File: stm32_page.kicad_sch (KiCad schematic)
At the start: 46 parts, among them J1 PZ254V-11-03P_C2937625, J2 PZ254V-11-03P_C2937625, J4 FTSH-107-01-L-DV-K-A, J5 PZ254V-11-03P_C2937625, SW2 6.0*6.0*6.0, SW3 6.0*6.0*6.0, U1 STM32L431KBU6_C2826408, U10 MAX3221ECPWR, X1 SC-32S32.768kHz20PPM7pF

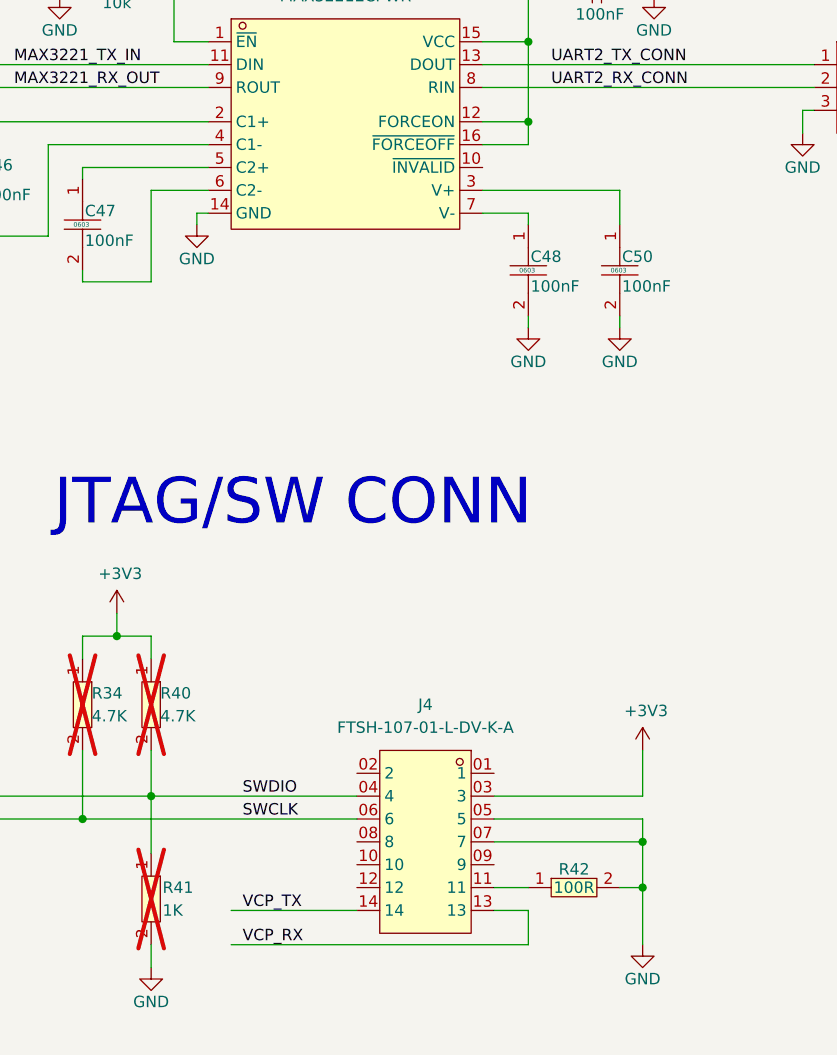
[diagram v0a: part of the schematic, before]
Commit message: replaced part for lower cost
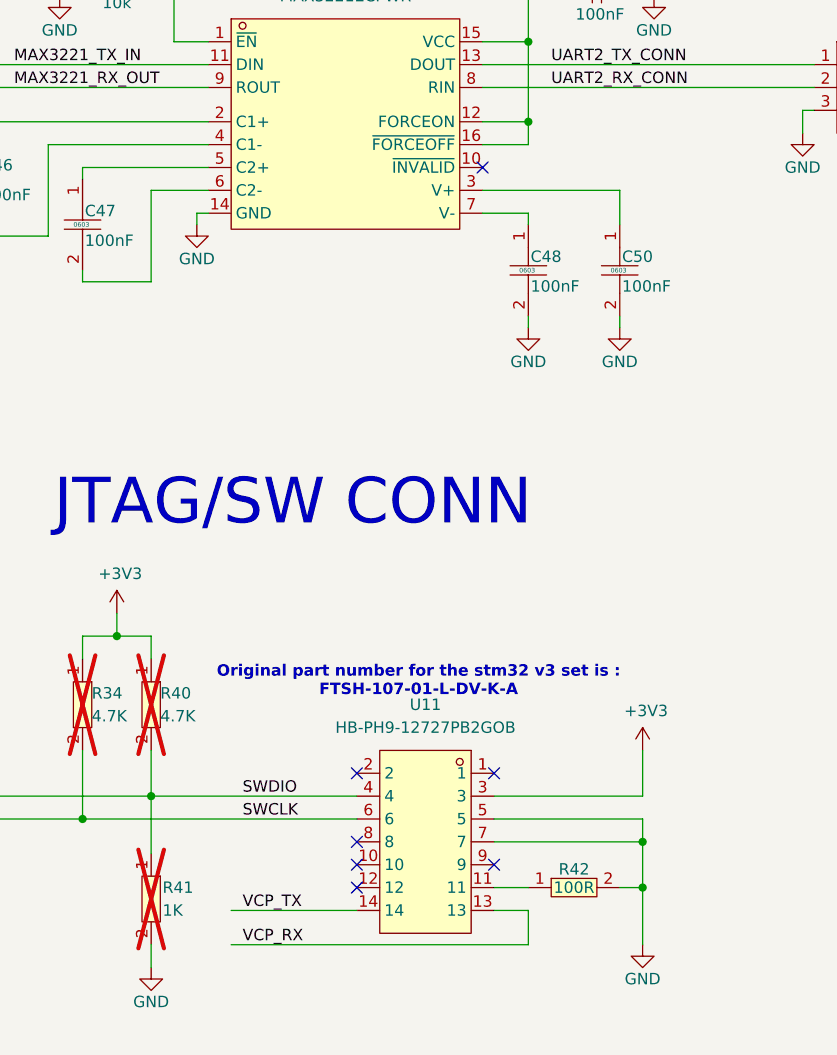
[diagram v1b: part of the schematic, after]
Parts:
- removed J4: FTSH-107-01-L-DV-K-A, easyeda2kicad:HDR-SMD_14P-P1.27_FTSH-107-01-L-DV-K-A, symbol easyeda2kicad:FTSH-107-01-L-DV-K-A
- added U11: HB-PH9-12727PB2GOB, easyeda2kicad:HDR-SMD_14P-P1.27-V-M-R2-C7-LS5.5, symbol easyeda2kicad:HB-PH9-12727PB2GOB
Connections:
- net +3V3: now also U11.3
- net GND: now also U11.5, U11.7
- net SWCLK: now also U11.6
- net SWDIO: now also U11.4
- net VCP_RX: now also U11.13
- net VCP_TX: now also U11.14
- net at R42.1: now also U11.11
- no-connect marks 0 -> 7
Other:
- note added: "Original part number for the stm32 v3 set is : FTSH-107-01-L-DV-K-A"
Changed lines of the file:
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@@
 		)
 	)
+	(text "Original part number for the stm32 v3 set is :\nFTSH-107-01-L-DV-K-A\n"
+		(exclude_from_sim no)
+		(at 338.328 208.28 0)
+		(effects
+			(font
+				(size 1.27 1.27)
+				(thickness 0.254)
+				(bold yes)
+			)
+		)
+	)
 	(text "VBAT"
 		(exclude_from_sim no)
@@
 		(color 0 0 0 0)
 	)
+	(no_connect
+		(at 331.47 228.6)
+	)
+	(no_connect
+		(at 331.47 218.44)
+	)
+	(no_connect
+		(at 346.71 218.44)
+	)
+	(no_connect
+		(at 345.44 151.13)
+	)
+	(no_connect
+		(at 331.47 231.14)
+	)
+	(no_connect
+		(at 331.47 226.06)
+	)
+	(no_connect
+		(at 346.71 228.6)
+	)
 	(wire
 		(pts
@@
 	)
 	(symbol
+		(lib_id "easyeda2kicad:HB-PH9-12727PB2GOB")
+		(at 339.09 226.06 0)
+		(mirror y)
+		(unit 1)
+		(exclude_from_sim no)
+		(in_bom yes)
+		(on_board yes)
+		(dnp no)
+		(property "Reference" "U11"
+			(at 339.09 210.82 0)
+			(effects
+				(font
+					(size 1.27 1.27)
+				)
+			)
+		)
+		(property "Value" "HB-PH9-12727PB2GOB"
+			(at 339.09 213.36 0)
+			(effects
+				(font
+					(size 1.27 1.27)
+				)
+			)
+		)
+		(property "Footprint" "easyeda2kicad:HDR-SMD_14P-P1.27-V-M-R2-C7-LS5.5"
+			(at 339.09 241.3 0)
+			(effects
+				(font
+					(size 1.27 1.27)
+				)
+				(hide yes)
+			)
+		)
+		(property "Datasheet" ""
+			(at 339.09 226.06 0)
+			(effects
+				(font
+					(size 1.27 1.27)
+				)
+				(hide yes)
+			)
+		)
+		(property "Description" ""
+			(at 339.09 226.06 0)
+			(effects
+				(font
+					(size 1.27 1.27)
+				)
+				(hide yes)
+			)
+		)
+		(property "LCSC Part" "C6332251"
+			(at 339.09 243.84 0)
+			(effects
+				(font
+					(size 1.27 1.27)
+				)
+				(hide yes)
+			)
+		)
+		(pin "10"
+		)
+		(pin "4"
+		)
+		(pin "7"
+		)
+		(pin "12"
+		)
+		(pin "13"
+		)
+		(pin "3"
+		)
+		(pin "11"
+		)
+		(pin "5"
+		)
+		(pin "9"
+		)
+		(pin "14"
+		)
+		(pin "1"
+		)
+		(pin "2"
+		)
+		(pin "8"
+		)
+		(pin "6"
+		)
+		(instances
+			(project ""
+				(path "/6657db5f-e034-448d-bae3-f44b9f033a3a/8c3def2f-5472-4ea2-874f-344fbccc06d4"
+					(reference "U11")
+					(unit 1)
+				)
+			)
+		)
+	)
+	(symbol
 		(lib_id "easyeda2kicad:CC0603KRX7R9BB104")
 		(at 350.52 162.56 270)
@@
 					(unit 1)
 				)
-			)
-		)
-	)
-	(symbol
-		(lib_id "easyeda2kicad:FTSH-107-01-L-DV-K-A")
-		(at 339.09 226.06 0)
-		(mirror y)
-		(unit 1)
-		(exclude_from_sim no)
-		(in_bom yes)
-		(on_board yes)
-		(dnp no)
-		(fields_autoplaced yes)
-		(property "Reference" "J4"
-			(at 339.09 210.82 0)
-			(effects
-				(font
-					(size 1.27 1.27)
-				)
-			)
-		)
-		(property "Value" "FTSH-107-01-L-DV-K-A"
-			(at 339.09 213.36 0)
-			(effects
-				(font
-					(size 1.27 1.27)
-				)
-			)
-		)
-		(property "Footprint" "easyeda2kicad:HDR-SMD_14P-P1.27_FTSH-107-01-L-DV-K-A"
-			(at 339.09 241.3 0)
-			(effects
-				(font
-					(size 1.27 1.27)
-				)
-				(hide yes)
-			)
-		)
-		(property "Datasheet" ""
-			(at 339.09 226.06 0)
-			(effects
-				(font
-					(size 1.27 1.27)
-				)
-				(hide yes)
-			)
-		)
-		(property "Description" ""
-			(at 339.09 226.06 0)
-			(effects
-				(font
-					(size 1.27 1.27)
-				)
-				(hide yes)
-			)
-		)
-		(property "LCSC Part" "C5563894"
-			(at 339.09 243.84 0)
-			(effects
-				(font
-					(size 1.27 1.27)
-				)
-				(hide yes)
-			)
-		)
-		(pin "13"
-		)
-		(pin "06"
-		)
-		(pin "14"
-		)
-		(pin "05"
-		)
-		(pin "08"
-		)
-		(pin "07"
-		)
-		(pin "09"
-		)
-		(pin "03"
-		)
-		(pin "01"
-		)
-		(pin "11"
-		)
-		(pin "10"
-		)
-		(pin "12"
-		)
-		(pin "02"
-		)
-		(pin "04"
-		)
-		(instances
-			(project "stm32"
-				(path "/6657db5f-e034-448d-bae3-f44b9f033a3a/8c3def2f-5472-4ea2-874f-344fbccc06d4"
-					(reference "J4")
-					(unit 1)
-				)

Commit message: removed 1uf cap
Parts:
- C42: now not fitted
- C43: now not fitted; now left out of the parts list
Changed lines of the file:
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@@
 		(at 59.69 33.02 270)
 		(unit 1)
-		(exclude_from_sim no)
+		(exclude_from_sim yes)
 		(in_bom yes)
-		(on_board yes)
-		(dnp no)
+		(on_board no)
+		(dnp yes)
 		(property "Reference" "C42"
 			(at 59.944 31.496 90)
@@
 		(at 67.31 33.02 270)
 		(unit 1)
-		(exclude_from_sim no)
-		(in_bom yes)
+		(exclude_from_sim yes)
+		(in_bom no)
 		(on_board yes)
-		(dnp no)
+		(dnp yes)
 		(property "Reference" "C43"
 			(at 67.564 31.496 90)

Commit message: Changed a bit component that where out of stock
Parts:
- C42: now fitted
- C43: now fitted; now in the parts list
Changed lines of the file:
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@@
 		(at 59.69 33.02 270)
 		(unit 1)
-		(exclude_from_sim yes)
+		(exclude_from_sim no)
 		(in_bom yes)
-		(on_board no)
-		(dnp yes)
+		(on_board yes)
+		(dnp no)
 		(property "Reference" "C42"
 			(at 59.944 31.496 90)
@@
 		(at 67.31 33.02 270)
 		(unit 1)
-		(exclude_from_sim yes)
-		(in_bom no)
+		(exclude_from_sim no)
+		(in_bom yes)
 		(on_board yes)
-		(dnp yes)
+		(dnp no)
 		(property "Reference" "C43"
 			(at 67.564 31.496 90)

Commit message: Removed VBAT wrong text on stm32 page
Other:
- note removed: "VBAT"
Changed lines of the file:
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@@
-		)
-	)
-	(text "VBAT"
-		(exclude_from_sim no)
-		(at 67.564 24.638 0)
-		(effects
-			(font
-				(size 1.27 1.27)
-			)
 		)
 	)

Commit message: Advanced placement , minor schem changes
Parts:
- removed R26, R27: 0603WAF0000T5E, easyeda2kicad:R0603, symbol easyeda2kicad:0603WAF0000T5E
- removed TP3, TP4: TestPoint, TestPoint:TestPoint_Pad_2.0x2.0mm, symbol Connector:TestPoint

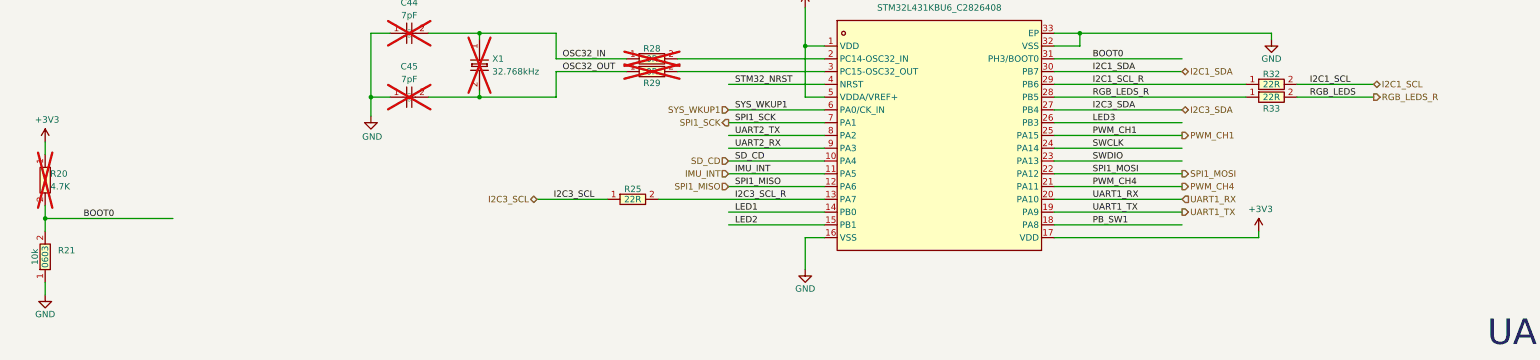
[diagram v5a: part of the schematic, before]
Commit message: Finished placement , added few TP's
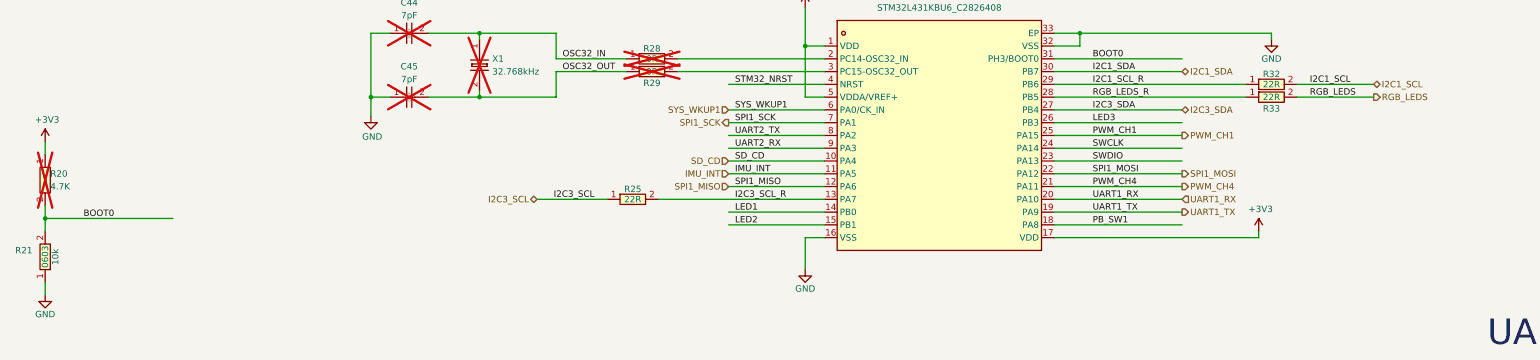
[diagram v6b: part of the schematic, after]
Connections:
- net RGB_LEDS_R: no longer R33.2
- new net RGB_LEDS: R33.2
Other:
- moved on the sheet: R21
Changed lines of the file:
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@@
 		)
 	)
-	(hierarchical_label "RGB_LEDS_R"
+	(hierarchical_label "RGB_LEDS"
 		(shape output)
 		(at 290.83 71.12 0)
@@
 	(symbol
 		(lib_id "easyeda2kicad:0603WAF1002T5E")
-		(at 26.67 102.87 90)
+		(at 26.67 102.87 270)
+		(mirror x)
 		(unit 1)
 		(exclude_from_sim no)
@@
 		(dnp no)
 		(property "Reference" "R21"
-			(at 29.21 101.5999 90)
+			(at 24.13 101.5999 90)
 			(effects
 				(font
@@
 		)
 		(property "Value" "0603WAF1002T5E"
-			(at 29.21 104.1399 90)
+			(at 24.13 104.1399 90)
 			(effects
 				(font
@@
 		)
 		(property "Footprint" "easyeda2kicad:R0603"
-			(at 34.29 102.87 0)
+			(at 19.05 102.87 0)
 			(effects
 				(font
@@
 		)
 		(property "Datasheet" "https://lcsc.com/product-detail/Chip-Resistor-Surface-Mount-UniOhm_10KR-1002-1_C25804.html"
-			(at 36.83 102.87 0)
+			(at 16.51 102.87 0)
 			(effects
 				(font
@@
 		)
 		(property "Description" "10k"
-			(at 24.638 102.87 0)
+			(at 28.702 102.87 0)
 			(effects
 				(font
@@
 		)
 		(property "LCSC Part" "C25804"
-			(at 39.37 102.87 0)
+			(at 13.97 102.87 0)
 			(effects
 				(font
